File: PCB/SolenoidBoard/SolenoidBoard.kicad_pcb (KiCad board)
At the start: 2 copper layers, 90 x 60 mm, 0 parts

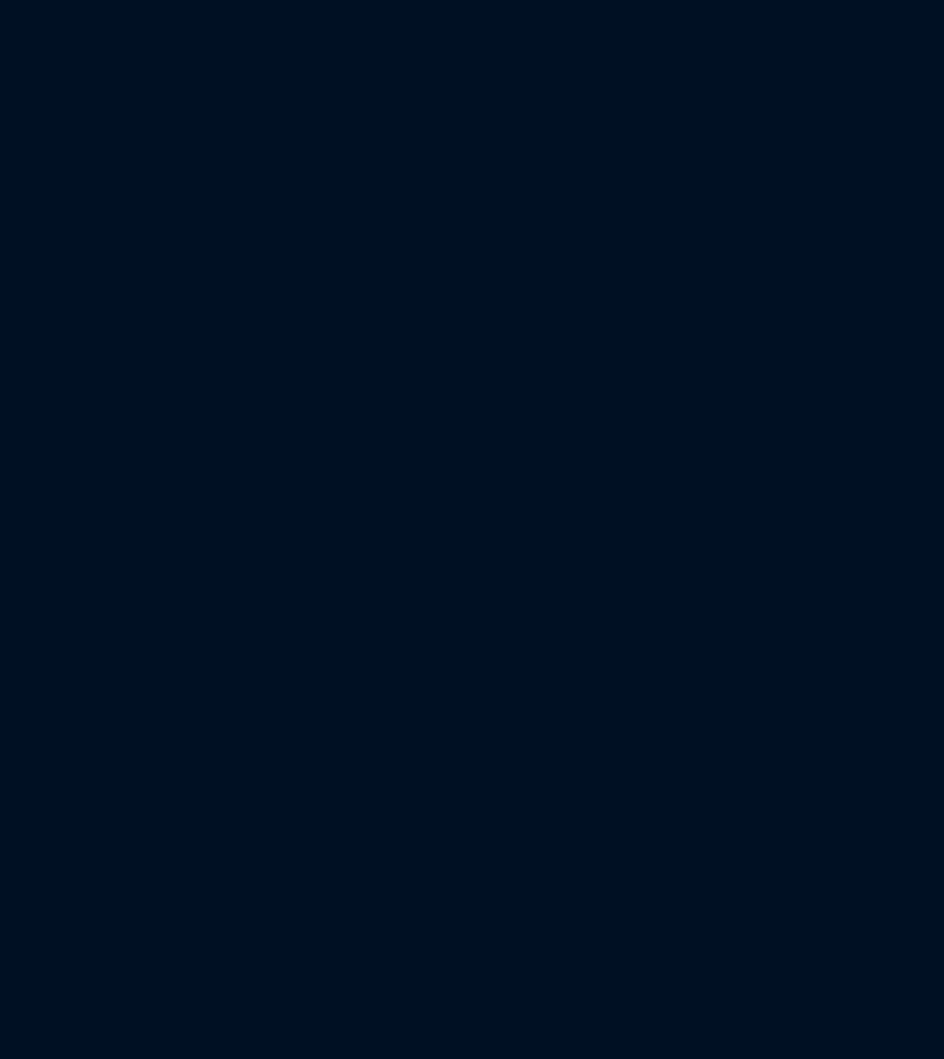
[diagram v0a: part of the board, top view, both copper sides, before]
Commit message: 昇圧部コピー
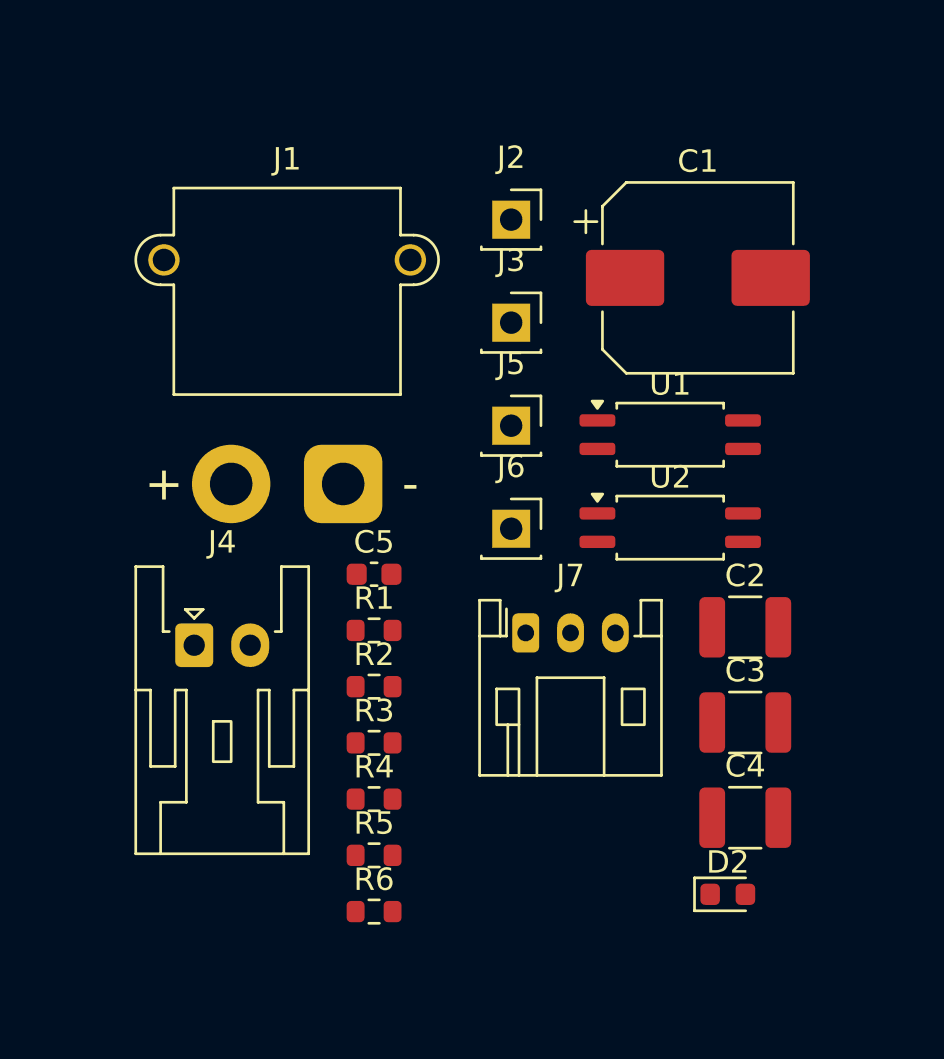
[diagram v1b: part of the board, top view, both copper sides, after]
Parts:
- added C1: 100u, Capacitor_SMD:CP_Elec_8x10, F.Cu at (141.2, 66.6)
- added C2: 10u, Capacitor_SMD:C_1210_3225Metric, F.Cu at (143.3, 82.2)
- added C3: 10u, Capacitor_SMD:C_1210_3225Metric, F.Cu at (143.3, 86.4)
- added C4: 10u, Capacitor_SMD:C_1210_3225Metric, F.Cu at (143.3, 90.7)
- added C5: 15p, Capacitor_SMD:C_0603_1608Metric, F.Cu at (126.7, 79.8)
- added D2: LED, LED_SMD:LED_0603_1608Metric, F.Cu at (142.5, 94.1)
- added J1: XT30, Connector_AMASS:AMASS_XT30PW-M_1x02_P2.50mm_Horizontal, F.Cu at (125.3, 75.8)
- added J2: Con_45V, Connector_PinSocket_2.54mm:PinSocket_1x01_P2.54mm_Vertical, F.Cu at (132.8, 64.0)
- added J3: Con_45V, Connector_PinSocket_2.54mm:PinSocket_1x01_P2.54mm_Vertical, F.Cu at (132.8, 68.6)
- added J4: Conn_01x02, Connector_JST:JST_XA_S02B-XASK-1_1x02_P2.50mm_Horizontal, F.Cu at (118.7, 83.0)
- added J5: Con_GND, Connector_PinSocket_2.54mm:PinSocket_1x01_P2.54mm_Vertical, F.Cu at (132.8, 73.2)
- added J6: Con_GND, Connector_PinSocket_2.54mm:PinSocket_1x01_P2.54mm_Vertical, F.Cu at (132.8, 77.8)
- added J7: Conn_01x03, Connector_JST:JST_PH_S3B-PH-K_1x03_P2.00mm_Horizontal, F.Cu at (133.5, 82.4)
- added R1: 10k, Resistor_SMD:R_0603_1608Metric, F.Cu at (126.7, 82.3)
- added R2: 10k, Resistor_SMD:R_0603_1608Metric, F.Cu at (126.7, 84.8)
- added R3: 1k, Resistor_SMD:R_0603_1608Metric, F.Cu at (126.7, 87.3)
- added R4: 10k, Resistor_SMD:R_0603_1608Metric, F.Cu at (126.7, 89.8)
- added R5: 330, Resistor_SMD:R_0603_1608Metric, F.Cu at (126.7, 92.4)
- added R6: 330, Resistor_SMD:R_0603_1608Metric, F.Cu at (126.7, 94.9)
- added U1: TLP293, Package_SO:SOIC-4_4.55x2.6mm_P1.27mm, F.Cu at (139.9, 73.6)
- added U2: TLP293, Package_SO:SOIC-4_4.55x2.6mm_P1.27mm, F.Cu at (139.9, 77.7)

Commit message: 回路図完成
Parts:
- added D1: CUHS20S60,H3F, Diode_SMD:D_SOD-323_HandSoldering, F.Cu at (169.3, 64.2)
- added IC1: NJW4132U2-B-TE2, Package_TO_SOT_SMD:SOT-89-5_Handsoldering, F.Cu at (155.6, 101.9)
- added L1: NR10050T470M, Inductor_SMD:L_10.4x10.4_H4.8, F.Cu at (157.5, 92.8)
- added Q1: Q_PMOS_GSD, Package_TO_SOT_SMD:SOT-23-3, F.Cu at (166.3, 89.1)
- added Q2: TPH11006NL,LQ_S, SOP Advance:SOP Advance, F.Cu at (161.8, 74.3)
- added R7: 330, Resistor_SMD:R_0603_1608Metric, F.Cu at (168.7, 66.9)
- added R8: 330, Resistor_SMD:R_0603_1608Metric, F.Cu at (168.7, 69.4)
- added RV1: 50k, Potentiometer_SMD:Potentiometer_Bourns_TC33X_Vertical, F.Cu at (169.2, 73.4)
- added S1: SKRPACE010, SKRPACE010:SW_SKRPACE010, F.Cu at (163.5, 101.2)
- added U3: TLP293, Package_SO:SOIC-4_4.55x2.6mm_P1.27mm, F.Cu at (161.9, 64.8)
- added U4: TLP293, Package_SO:SOIC-4_4.55x2.6mm_P1.27mm, F.Cu at (161.9, 68.9)

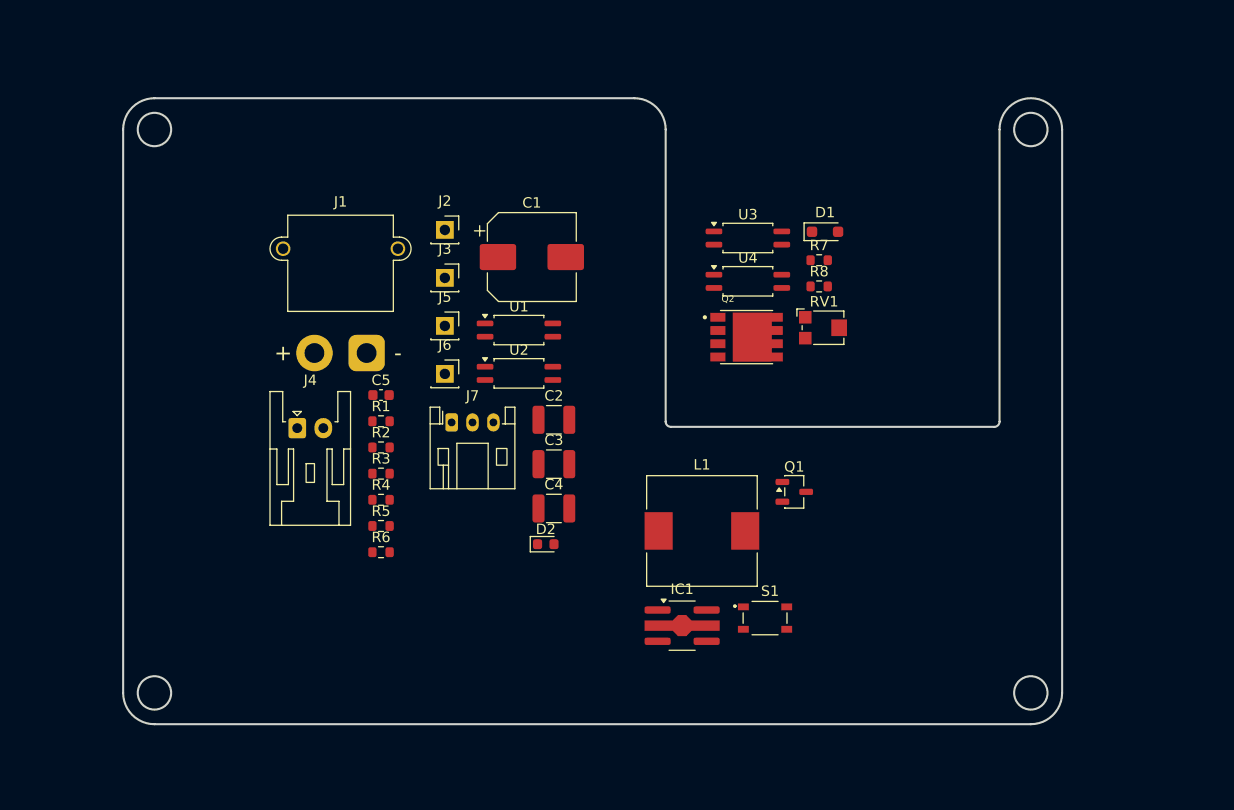
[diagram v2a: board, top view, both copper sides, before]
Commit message: 部品配置終わり
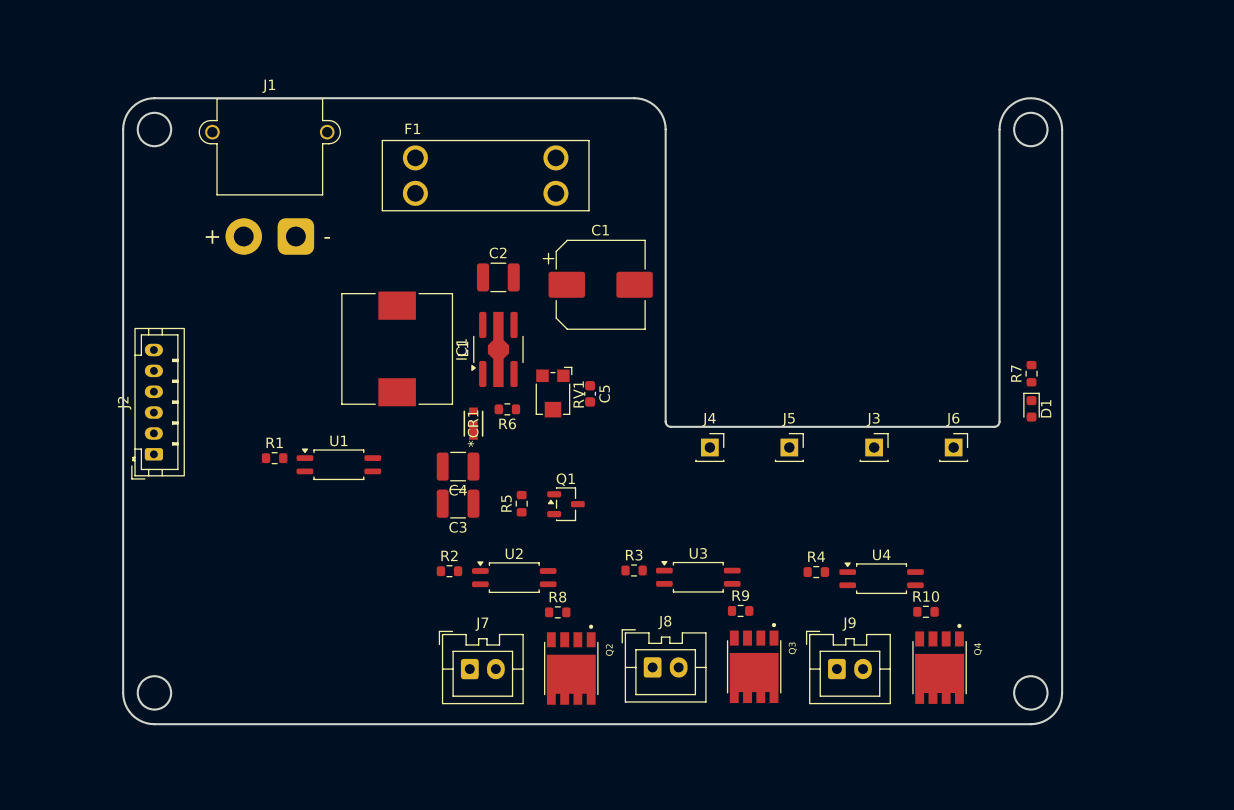
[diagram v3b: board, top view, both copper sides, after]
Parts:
- removed D2: LED, LED_SMD:LED_0603_1608Metric
- removed S1: SKRPACE010, SKRPACE010:SW_SKRPACE010
- added CR1: CUHS20S60_H3F, CUHS20S60:SOD-323HEUS2H_TOS, F.Cu at (135.6, 82.5)
- added F1: 3557-15, 3557-15:FUSE_3557-15, F.Cu at (136.8, 58.8)
- added J8: Conn_01x02, Connector_JST:JST_XA_B02B-XASK-1_1x02_P2.50mm_Vertical, F.Cu at (152.8, 105.9)
- added J9: Conn_01x02, Connector_JST:JST_XA_B02B-XASK-1_1x02_P2.50mm_Vertical, F.Cu at (170.4, 106.1)
- added Q3: TPH11006NL,LQ_S, SOP Advance:SOP Advance, F.Cu at (162.5, 105.9)
- added Q4: TPH11006NL,LQ_S, SOP Advance:SOP Advance, F.Cu at (180.3, 105.9)
- added R10: 10k, Resistor_SMD:R_0603_1608Metric, F.Cu at (179.0, 100.6)
- added R9: 10k, Resistor_SMD:R_0603_1608Metric, F.Cu at (161.2, 100.5)
- D1: value CUHS20S60,H3F -> LED; footprint Diode_SMD:D_SOD-323_HandSoldering -> LED_SMD:LED_0603_1608Metric
- J2: value Con_45V -> Conn_01x06_Pin; footprint Connector_PinSocket_2.54mm:PinSocket_1x01_P2.54mm_Vertical -> Connector_JST:JST_PH_B6B-PH-K_1x06_P2.00mm_Vertical
- J4: value Conn_01x02 -> Con_45V; footprint Connector_JST:JST_XA_S02B-XASK-1_1x02_P2.50mm_Horizontal -> Connector_PinSocket_2.54mm:PinSocket_1x01_P2.54mm_Vertical
- J7: value Conn_01x03 -> Conn_01x02; footprint Connector_JST:JST_PH_S3B-PH-K_1x03_P2.00mm_Horizontal -> Connector_JST:JST_XA_B02B-XASK-1_1x02_P2.50mm_Vertical
- R1, R2, R4: value 10k -> 330
- R3: value 1k -> 330
- R5, R7, R8: value 330 -> 10k
- R6: value 330 -> 1k
- moved J6 49.3 mm to (181.6, 84.8)
- moved J3 44.2 mm to (174.0, 84.8)
- moved R4 42.3 mm to (168.4, 96.8)
- moved R8 40.0 mm to (143.7, 100.6)
- moved J4 39.6 mm to (158.2, 84.8)
- moved Q2 35.9 mm to (145.0, 106.0), turned to -90 degrees
- moved J2 35.2 mm to (105.0, 85.5), turned to 90 degrees
- moved J5 35.0 mm to (165.9, 84.8)
- moved L1 34.0 mm to (128.3, 75.4), turned to -90 degrees
- moved U3 32.9 mm to (157.1, 97.3)
- moved IC1 31.8 mm to (138.0, 75.4), turned to 90 degrees
- moved U4 31.3 mm to (174.7, 97.4)
- moved RV1 26.8 mm to (143.2, 79.8), turned to -90 degrees
- moved D1 26.1 mm to (189.1, 81.1), turned to -90 degrees
- moved R3 26.0 mm to (151.0, 96.6)
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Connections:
- D1 pad 1: +48V -> Net-(D1-K)
- IC1 pad 1: Net-(D1-A) -> Net-(IC1-SW)
- J1 pad 2: +12V -> Net-(J1-Pin_2)
- J2 pad 1: Net-(D2-A) -> GND
- J3 pad 1: Net-(D2-A) -> Net-(D1-A)
- J4 pad 1: Net-(D2-A) -> Net-(D1-A)
- J7 pad 1: GND -> Net-(D1-A)
- J7 pad 2: /Pch -> Net-(J7-Pin_2)
- L1 pad 2: Net-(D1-A) -> Net-(IC1-SW)
- Q1 pad 3: Net-(D2-A) -> Net-(D1-A)
- Q2 pad 4: /Nch_G -> /Nch_R_G
- Q2 pad 5: Net-(J4-Pin_2) -> Net-(J7-Pin_2)
- Q2 pad 6: Net-(J4-Pin_2) -> Net-(J7-Pin_2)
- Q2 pad 7: Net-(J4-Pin_2) -> Net-(J7-Pin_2)
- Q2 pad 8: Net-(J4-Pin_2) -> Net-(J7-Pin_2)
- Q2 pad 9: Net-(J4-Pin_2) -> Net-(J7-Pin_2)
- R1 pad 1: +48V -> /Pch
- R1 pad 2: /Pch_G -> Net-(R1-Pad2)
- R2 pad 1: Net-(D2-K) -> /Nch_R
- R2 pad 2: GND -> Net-(R2-Pad2)
- R3 pad 1: Net-(IC1-IN-) -> /Nch_C
- R3 pad 2: GND -> Net-(R3-Pad2)
- R4 pad 1: /Nch_G -> /Nch_L
- R4 pad 2: GND -> Net-(R4-Pad2)
- R5 pad 1: /Pch -> +48V
- R5 pad 2: Net-(R5-Pad2) -> /Pch_G
- R6 pad 1: /Nch -> Net-(IC1-IN-)
- R6 pad 2: Net-(R6-Pad2) -> GND
- R7 pad 1: /Nch -> Net-(D1-K)
- R7 pad 2: Net-(R7-Pad2) -> GND
- R8 pad 1: /Nch -> /Nch_R_G
- R8 pad 2: Net-(R8-Pad2) -> GND
- U1 pad 1: Net-(R5-Pad2) -> Net-(R1-Pad2)
- U2 pad 1: Net-(R6-Pad2) -> Net-(R2-Pad2)
- U2 pad 3: /Nch_G -> /Nch_R_G
- U3 pad 1: Net-(R7-Pad2) -> Net-(R3-Pad2)
- U3 pad 3: /Nch_G -> /Nch_C_G
- U4 pad 1: Net-(R8-Pad2) -> Net-(R4-Pad2)
- U4 pad 3: /Nch_G -> /Nch_L_G

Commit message: 配線ラフ終わり
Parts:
- moved J2 13.2 mm to (109.0, 73.0), turned to -90 degrees
- moved Q3 4.45 mm to (158.6, 103.6)
- moved Q4 4.45 mm to (176.4, 103.7)
- moved R2 4.45 mm to (129.4, 94.5)
- moved Q2 4.45 mm to (141.1, 103.8)
- moved R8 4.45 mm to (139.8, 98.4)
- moved R9 4.45 mm to (157.3, 98.3)
- moved U3 4.45 mm to (153.3, 95.1)
- moved R10 4.45 mm to (175.1, 98.4)
- moved R3 4.45 mm to (147.1, 94.4)
- moved R4 4.45 mm to (164.6, 94.6)
- moved U2 4.45 mm to (135.6, 95.1)
- moved U4 4.45 mm to (170.8, 95.2)
- moved J7 3.00 mm to (133.1, 108.2), turned to 90 degrees
- moved J8 2.94 mm to (150.9, 108.2), turned to 90 degrees
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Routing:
- net GND: track 0.00 -> 281.6 mm, vias 0 -> 11
- net Net-(D1-A): track 0.00 -> 122.9 mm, vias 0 -> 1
- net +48V: track 0.00 -> 76.3 mm, vias 0 -> 2
- net /Nch_L: track 0.00 -> 60.4 mm, vias 0 -> 2
- net +12V: track 0.00 -> 49.3 mm, vias 0 -> 2
- net /Nch_C: track 0.00 -> 43.4 mm, vias 0 -> 2
- net /Nch_R: track 0.00 -> 26.8 mm
- net Net-(J1-Pin_2): track 0.00 -> 23.0 mm
- net /Pch_G: track 0.00 -> 18.9 mm, vias 0 -> 2
- net Net-(IC1-IN-): track 0.00 -> 14.6 mm
- net Net-(IC1-SW): track 0.00 -> 13.3 mm
- net /Pch: track 0.00 -> 11.6 mm
- net Net-(J7-Pin_2): track 0.00 -> 8.93 mm
- net Net-(J9-Pin_2): track 0.00 -> 8.91 mm
- net Net-(J8-Pin_2): track 0.00 -> 8.37 mm
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
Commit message: 配線終わり
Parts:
- Q1: value Q_PMOS_GSD -> Q_PMOS_GDS; footprint Package_TO_SOT_SMD:SOT-23-3 -> Package_TO_SOT_SMD:TO-252-2
- moved R4 4.09 mm to (168.1, 92.5)
- moved Q1 3.71 mm to (147.9, 89.0)
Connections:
- Q1 pad 2: +48V -> Net-(D1-A)
- Q1 pad 3: Net-(D1-A) -> +48V
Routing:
- net /Nch_L: track 60.4 -> 64.8 mm
- net GND: track 281.6 -> 284.8 mm
- net Net-(D1-A): track 122.9 -> 120.2 mm
- net +12V: track 49.3 -> 50.6 mm
- net /Pch_G: track 18.9 -> 19.6 mm
- net +48V: track 76.3 -> 75.8 mm, vias 2 -> 4
- added copper zone on F.Cu, net +12V
- added copper zone on F.Cu, net +48V
- added copper zone on B.Cu, net GND
- added copper zone on F.Cu, net GND
- added copper zone on B.Cu, net Net-(D1-A)
- added copper zone on F.Cu, net Net-(D1-A)
- added copper zone on F.Cu, net Net-(IC1-SW)
- added copper zone on F.Cu, net Net-(J1-Pin_2)

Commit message: ソレノイド基板完成
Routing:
- net GND: track 284.8 -> 286.8 mm, vias 11 -> 238
- net Net-(D1-A): vias 1 -> 4
- added copper zone on F.Cu, net Net-(J7-Pin_2)
- added copper zone on F.Cu, net Net-(J8-Pin_2)
- added copper zone on F.Cu, net Net-(J9-Pin_2)

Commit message: 電圧系追加
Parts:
- added GND: Conn_01x01_Pin, TestPoint:TestPoint_Loop_D2.50mm_Drill1.0mm, F.Cu at (124.5, 106.3)
- added VIN: Conn_01x01_Pin, TestPoint:TestPoint_Loop_D2.50mm_Drill1.0mm, F.Cu at (120.0, 106.2)
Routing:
- net +12V: track 50.6 -> 91.8 mm
- net GND: track 286.8 -> 295.5 mm

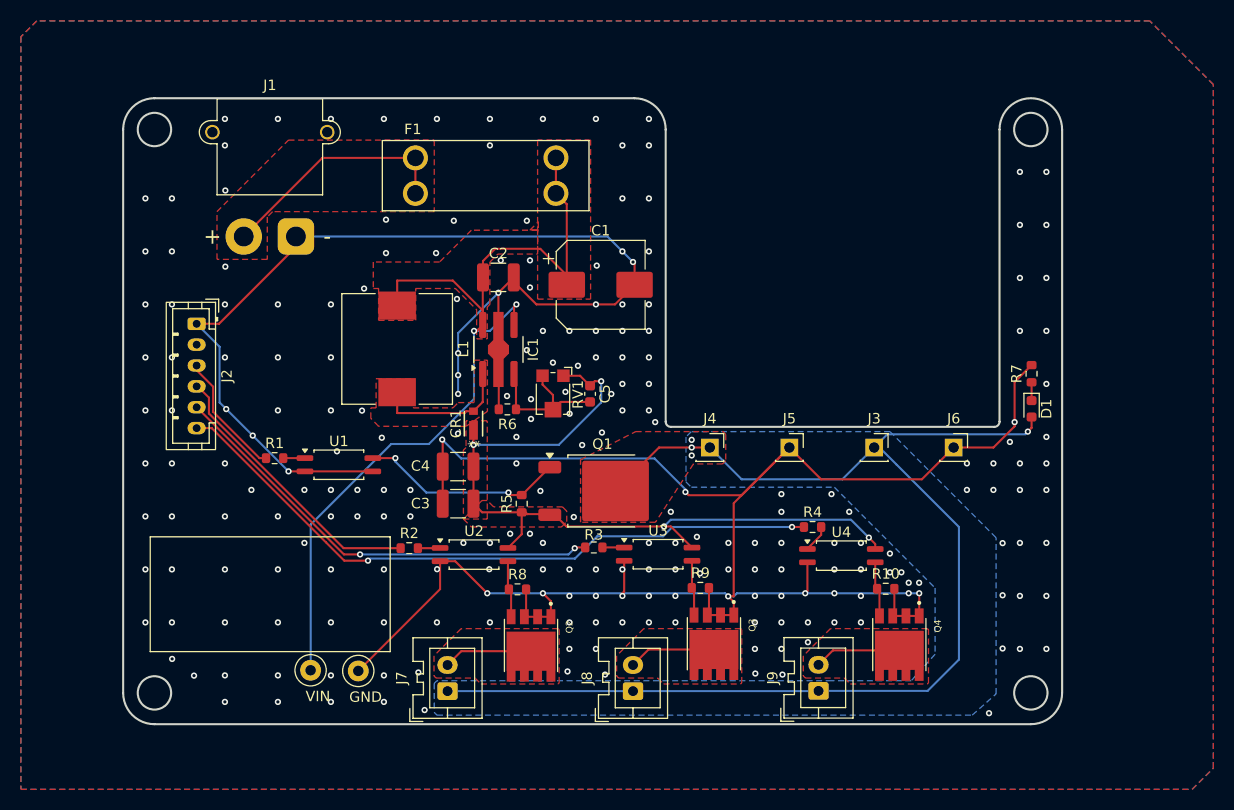
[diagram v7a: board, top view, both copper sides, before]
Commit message: 基板外形変更
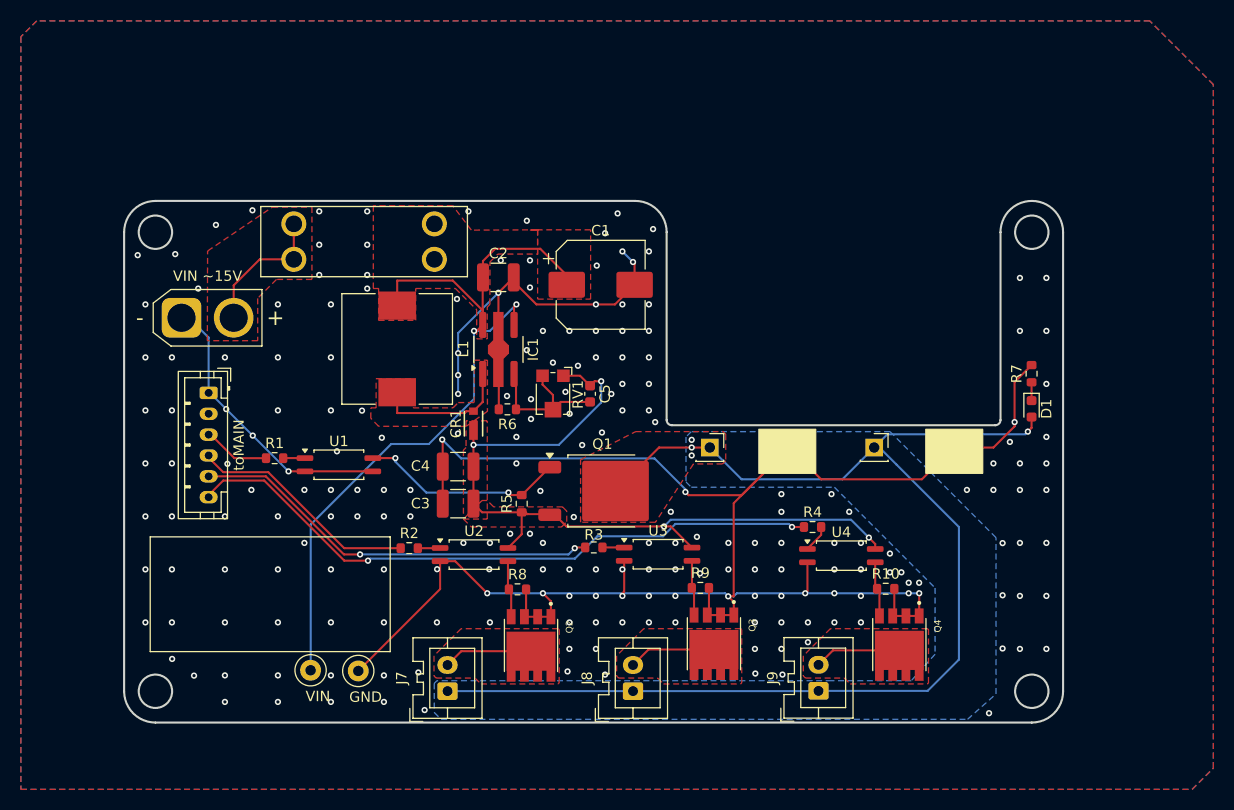
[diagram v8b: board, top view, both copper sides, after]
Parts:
- VIN ~15V: renamed from J1; footprint Connector_AMASS:AMASS_XT30PW-M_1x02_P2.50mm_Horizontal -> Connector_AMASS:AMASS_XT30U-M_1x02_P5.0mm_Vertical
- moved VIN ~15V 13.4 mm to (107.6, 72.4)
- moved F1 13.3 mm to (125.1, 65.1)
- moved toMAIN 6.72 mm to (110.2, 79.6)
- renumbered J2 to toMAIN
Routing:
- net GND: track 295.5 -> 251.7 mm, vias 238 -> 222
- net +12V: track 91.8 -> 79.2 mm
- net Net-(J1-Pin_2): track 23.0 -> 13.3 mm
- net /Pch: track 12.0 -> 6.44 mm
- net /Nch_R: track 26.9 -> 22.2 mm
- net /Nch_C: track 43.4 -> 39.5 mm
- net /Nch_L: track 64.8 -> 62.6 mm
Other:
- board size 90 x 60 mm -> 90 x 50 mm
